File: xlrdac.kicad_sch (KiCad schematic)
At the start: 19 parts, among them J1 Screw_Terminal_01x01, J2 Right Output, J3 Left Output, J4 Audio Stereo Input, U1 THAT1646, U2 THAT1646

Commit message: Rework grounding, export side view
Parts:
- removed J1: Screw_Terminal_01x01, TerminalBlock_MetzConnect:TerminalBlock_MetzConnect_360271_1x01_Horizontal_ScrewM3.0_Boxed, symbol Connector:Screw_Terminal_01x01
- removed J4: Audio Stereo Input, Connector_Audio:Jack_3.5mm_CUI_SJ-3523-SMT_Horizontal, symbol Connector:AudioJack3
- added C10, C11, C12, C9: (no value), symbol Device:C
- added J1: (no value), symbol Connector:AudioJack3
- added J4: (no value), symbol Connector:Screw_Terminal_01x03
- added R1: (no value), symbol Device:R
- added R2, R3: 0R, symbol Device:R
- added R4: 0R, Resistor_THT:R_Axial_DIN0204_L3.6mm_D1.6mm_P7.62mm_Horizontal, symbol Device:R
- J2: value Right Output -> (none)
- J3: value Left Output -> (none)
- N1: value Housing_Pad -> (none)
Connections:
- net VCC: now also C10.2, C12.2, R2.2
- net VEE: now also C11.1, C9.1, R3.2
- net at U1.4 (IN1): now also J1.T
- net at U2.4 (IN1): now also J1.R
- removed net Earth_Clean: C1.2, C2.2, C3.1, C4.1, J2.1, J2.G, J3.1, J3.G, N1.1 (PAD), U1.3 (GND), U2.3 (GND)
- new net: C1.2, C2.2, J2.1, J2.G
- new net: C3.1, C4.1, J3.1, J3.G
- new net GNDA: J1.S, R4.2, U1.3 (GND), U2.3 (GND)
- new net GNDPWR: C10.1, C11.2, C12.1, C9.2, R1.2, R4.1
- new net PWR.GND: J4.2 (Pin_2), N1.1 (PAD), R1.1
- new net PWR.VCC: J4.1 (Pin_1), R2.1
- new net PWR.VEE: J4.3 (Pin_3), R3.1
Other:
- moved on the sheet: N1

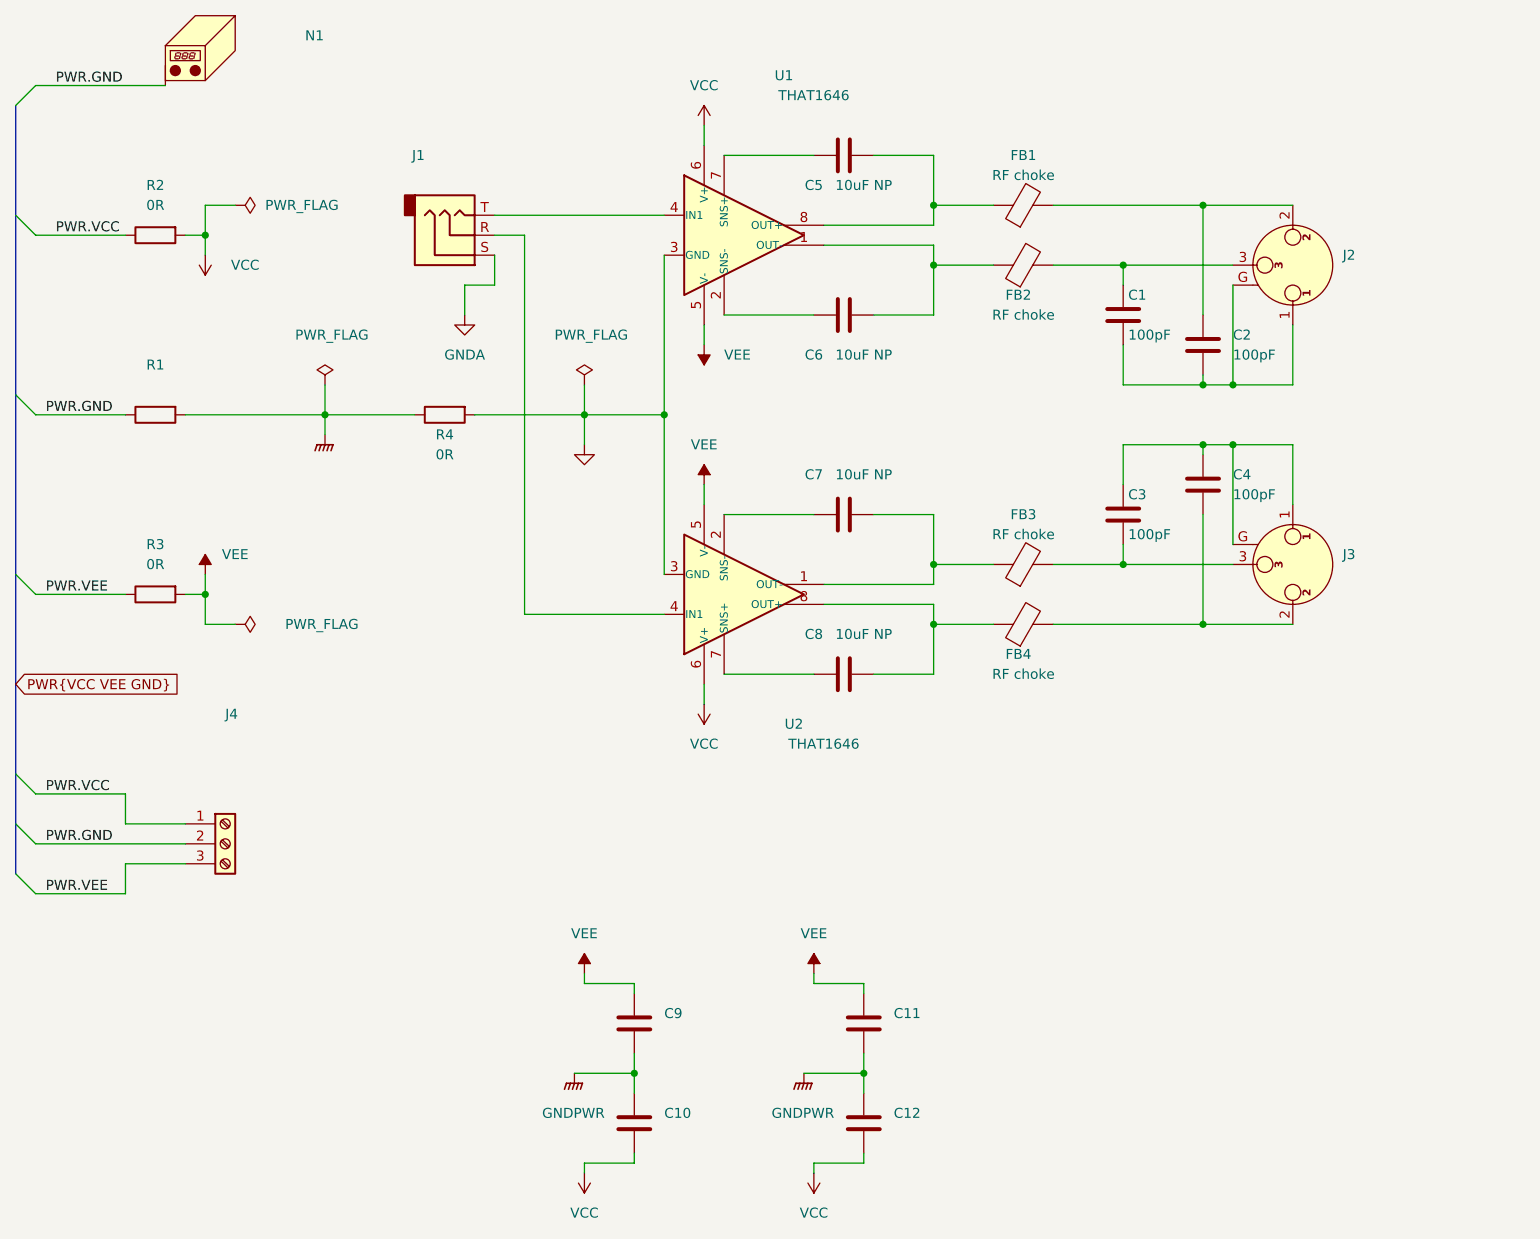
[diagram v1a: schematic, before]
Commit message: Move line drivers to dedicated file
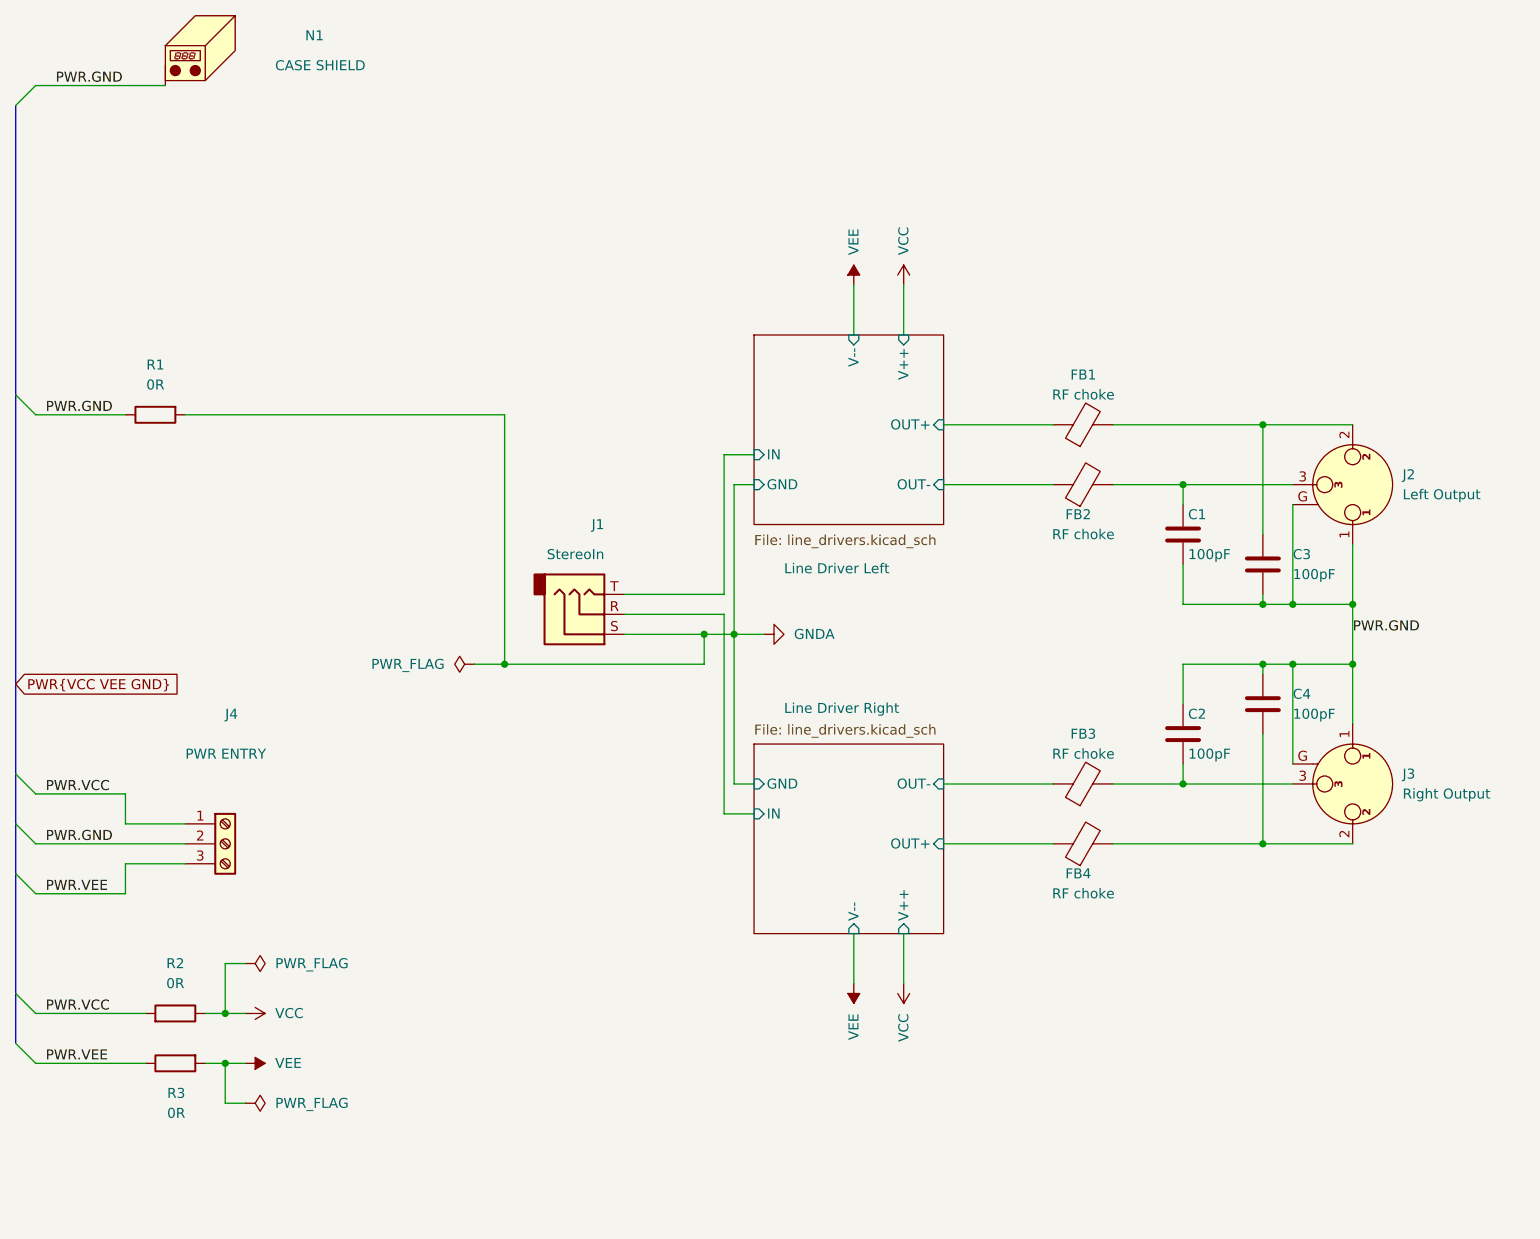
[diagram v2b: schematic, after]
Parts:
- removed C10, C11, C12, C9: (no value), symbol Device:C
- removed C5, C6, C7, C8: 10uF NP, Capacitor_THT:C_Radial_D6.3mm_H11.0mm_P2.50mm, symbol Device:C
- removed R4: 0R, Resistor_THT:R_Axial_DIN0204_L3.6mm_D1.6mm_P7.62mm_Horizontal, symbol Device:R
- removed U1, U2: THAT1646, Package_DIP:DIP-8_W7.62mm_Socket_LongPads, symbol nedko:THAT1646
- J1: value (none) -> StereoIn; footprint (none) -> Connector_Audio:Jack_3.5mm_CUI_SJ-3523-SMT_Horizontal
- J2: value (none) -> Left Output
- J3: value (none) -> Right Output
- J4: value (none) -> PWR ENTRY; footprint (none) -> Connector_Wire:SolderWire-1.5sqmm_1x03_P6mm_D1.7mm_OD3mm
- N1: value (none) -> CASE SHIELD
- R1: value (none) -> 0R; footprint (none) -> Resistor_THT:R_Axial_DIN0204_L3.6mm_D1.6mm_P7.62mm_Horizontal
- R2, R3: footprint (none) -> Resistor_THT:R_Axial_DIN0204_L3.6mm_D1.6mm_P7.62mm_Horizontal
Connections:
- net GNDPWR is gone; now on net GNDA: R1.2
- net PWR.GND: now also C1.2, C2.1, C3.2, C4.1, J2.1, J2.G, J3.1, J3.G
- net PWR.VCC: now also R3.2; no longer R2.1
- net PWR.VEE: now also R2.1; no longer R3.1
- net VCC: now also R3.1; no longer R2.2
- net VEE: now also R2.2; no longer R3.2
- net Line Driver Left/OUT-: now reaches FB2.1
- net Line Driver Left/IN: now reaches J1.T
- net Line Driver Left/OUT+: now reaches FB1.1
- net at FB1.2, J2.2: now also C3.1; no longer C2.1
- net at FB3.2, J3.3: now also C2.2; no longer C3.2
- net Line Driver Right/OUT-: now reaches FB3.1
- net Line Driver Right/IN: now reaches J1.R
- net Line Driver Right/OUT+: now reaches FB4.1
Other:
- added sheet Line Driver Left (line_drivers.kicad_sch)
- added sheet Line Driver Right (line_drivers.kicad_sch)
- moved on the sheet: J1
